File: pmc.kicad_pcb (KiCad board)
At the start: 6 copper layers, 52.1 x 93.3 mm, 167 parts, among them M1 TPS61040, M2 LM46001, M3 STM32F405RG, M4 REF3033, M5 TPS73633, M6 SN65HVD256, M7 UCC27211A, M8 UCC27211A, M9 UCC27211A, P1 FAN, P10 F1, P11 F2, P12 A1, P13 A2, P14 BOOT, P15 F1, P16 F2, P17 A1, P18 A2, P19 CONN4, P2 NTC, P20 CONN4, P21 CONN4, P22 CONN4, P23 CONN4, P3 HALL, P4 SPI, P5 PPM, P6 ANALOG, P7 CAN, P8 SWD, P9 USART, Q1 IRLML6401, Q2 IPT007N06N, Q3 IPT007N06N, Q4 IPT007N06N, Q5 IPT007N06N, Q6 IPT007N06N, Q7 IPT007N06N, U1 AD8539, U2 AD8539, U3 AD8417, U4 AD8417

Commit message: New mosfet driver and current sensing amp.
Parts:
- M7, M8, M9: value UCC27211A -> UCC27201A
- R47, R48: value 0.0003 1% -> 0.0005 1%
- U3, U4: value AD8417 -> AD8418
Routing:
- net GND: track 444.6 -> 445.9 mm, vias 228 -> 229
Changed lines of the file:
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@@
     (links 448)
     (no_connects 7)
-    (area 59.49 61.435 123.42 160.7915)
+    (area 60.249999 67.234999 112.470001 160.730001)
     (thickness 2)
     (drawings 109)
-    (tracks 2088)
+    (tracks 2091)
     (zones 0)
     (modules 167)
@@
   (title_block
     (title "Phobia Motor Controller")
-    (date 2019-04-27)
+    (date 2019-06-02)
     (rev 4c)
     (company "Roman Belov")
@@
   )
   (setup
-    (last_trace_width 0.508)
+    (last_trace_width 0.254)
     (user_trace_width 0.381)
     (user_trace_width 0.508)
@@
       (effects (font (size 0.635 0.635) (thickness 0.127)))
     )
-    (fp_text value UCC27211A (at 0 3.048 270) (layer F.SilkS) hide
+    (fp_text value UCC27201A (at 0 3.048 270) (layer F.SilkS) hide
       (effects (font (size 0.635 0.635) (thickness 0.127)))
     )
@@
       (effects (font (size 0.635 0.635) (thickness 0.127)))
     )
-    (fp_text value UCC27211A (at 0 3.048 270) (layer F.SilkS) hide
+    (fp_text value UCC27201A (at 0 3.048 270) (layer F.SilkS) hide
       (effects (font (size 0.635 0.635) (thickness 0.127)))
     )
@@
       (effects (font (size 0.635 0.635) (thickness 0.127)))
     )
-    (fp_text value UCC27211A (at -3.175 -5.08 270) (layer F.SilkS)
+    (fp_text value UCC27201A (at -3.175 -5.08 270) (layer F.SilkS)
       (effects (font (size 0.635 0.635) (thickness 0.127)))
     )
@@
       (effects (font (size 0.635 0.635) (thickness 0.127)))
     )
-    (fp_text value AD8417 (at 3.81 0 180) (layer F.SilkS)
+    (fp_text value AD8418 (at 3.81 0 180) (layer F.SilkS)
       (effects (font (size 0.635 0.635) (thickness 0.127)))
     )
@@
       (effects (font (size 0.635 0.635) (thickness 0.127)))
     )
-    (fp_text value AD8417 (at 3.81 0 180) (layer F.SilkS)
+    (fp_text value AD8418 (at 3.81 0 180) (layer F.SilkS)
       (effects (font (size 0.635 0.635) (thickness 0.127)))
     )
@@
       (effects (font (size 0.635 0.635) (thickness 0.127)))
     )
-    (fp_text value "0.0003 1%" (at 0.635 0.254 360) (layer F.SilkS)
+    (fp_text value "0.0005 1%" (at 0.635 0.254 360) (layer F.SilkS)
       (effects (font (size 0.635 0.635) (thickness 0.127)))
     )
@@
       (effects (font (size 0.635 0.635) (thickness 0.127)))
     )
-    (fp_text value "0.0003 1%" (at 0.635 0.254 360) (layer F.SilkS)
+    (fp_text value "0.0005 1%" (at 0.635 0.254 360) (layer F.SilkS)
       (effects (font (size 0.635 0.635) (thickness 0.127)))
     )
@@
   (segment (start 104.775 139.3825) (end 102.997 139.3825) (width 0.254) (layer F.Cu) (net 47))
   (segment (start 102.997 139.3825) (end 102.87 139.5095) (width 0.254) (layer F.Cu) (net 47))
+  (segment (start 69.723 135.255) (end 69.723 136.398) (width 0.254) (layer F.Cu) (net 49))
+  (segment (start 69.723 136.398) (end 69.85 136.525) (width 0.254) (layer F.Cu) (net 49))
+  (via (at 69.85 136.525) (size 0.300001) (drill 0.3) (layers F.Cu B.Cu) (net 49))
   (segment (start 74.4855 108.712) (end 76.0095 108.712) (width 0.381) (layer B.Cu) (net 49))
   (segment (start 76.0095 105.8545) (end 76.0095 108.712) (width 0.381) (layer B.Cu) (net 49))

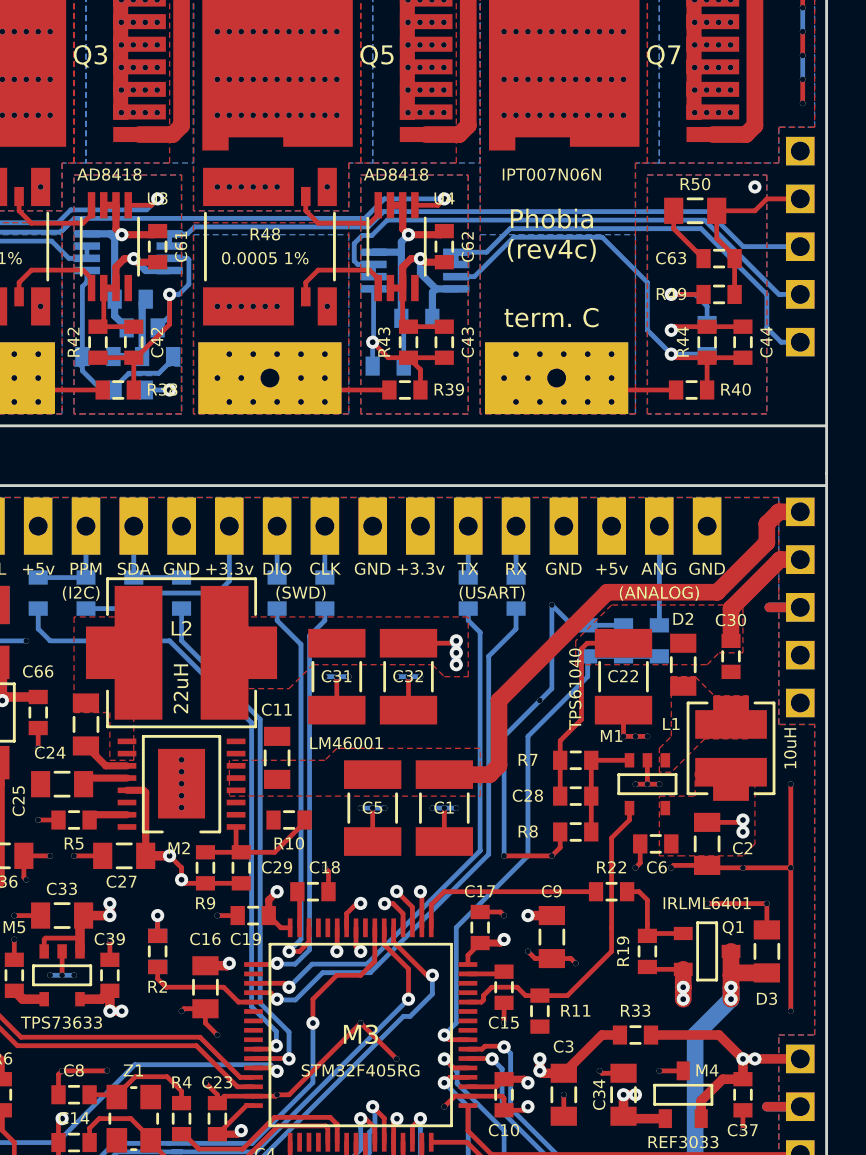
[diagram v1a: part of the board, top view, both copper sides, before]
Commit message: Two analog channels.
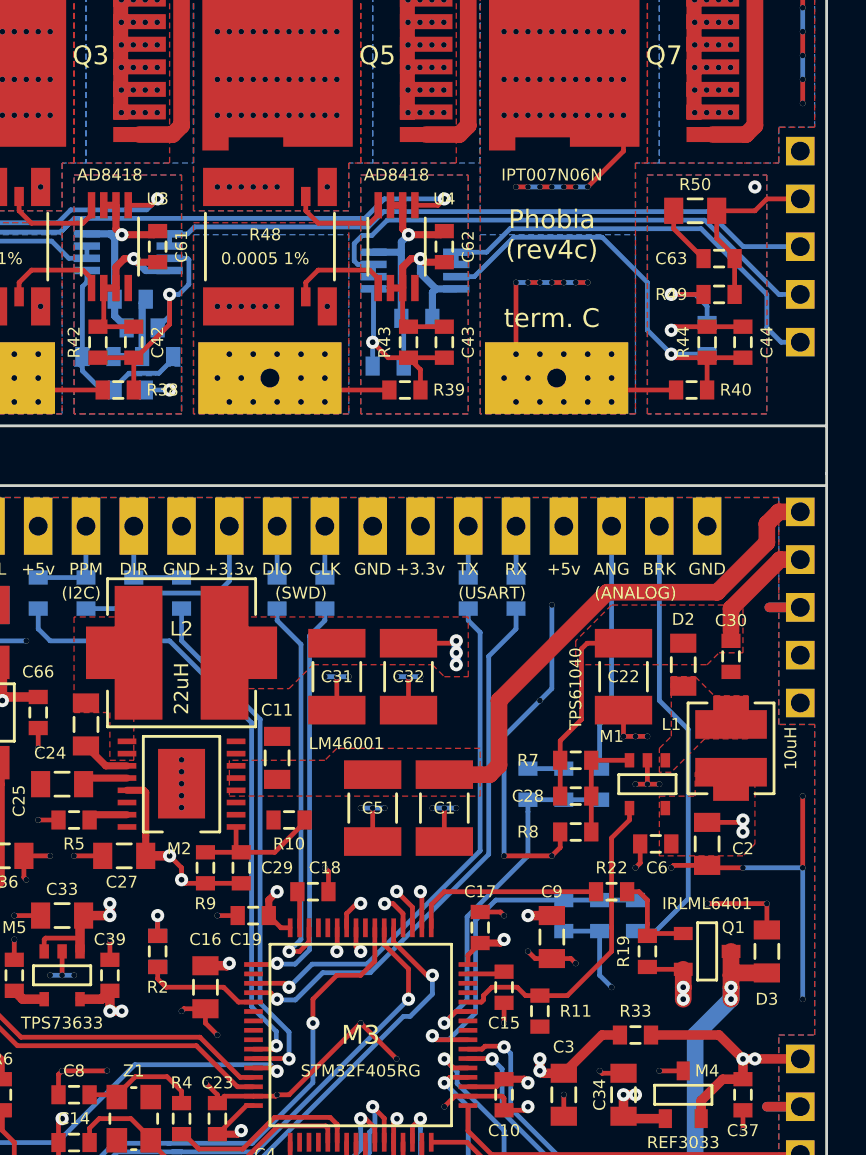
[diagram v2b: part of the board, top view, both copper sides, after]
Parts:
- added C67: 10nF 25v, foot:SM-0603, B.Cu at (98.4, 138.4)
- added R53: 10K 1%, foot:SM-0603, B.Cu at (100.3, 138.4)
- added R54: 10K 1%, foot:SM-0603, B.Cu at (102.2, 138.4)
- P6: footprint foot:PLS-3 -> foot:PLS-4
- P9: footprint foot:PLS-4 -> foot:PLS-3
- moved C40 8.25 mm to (96.5, 131.4)
- moved R34 8.25 mm to (98.4, 131.4)
- moved R36 8.25 mm to (100.3, 131.4)
- moved P6 1.27 mm to (102.2, 117.7)
- moved P9 1.27 mm to (93.3, 117.7)
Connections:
- C40 pad 2: ADC_IN14 -> ADC_IN9
- M3 pad 27: Net-(M3-Pad27) -> ADC_IN9
- P6 pad 3: GND -> Net-(P6-Pad3)
- R34 pad 2: ADC_IN14 -> ADC_IN9
- R36 pad 1: ADC_IN14 -> ADC_IN9
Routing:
- net Net-(P6-Pad3): track 0.00 -> 24.0 mm
- net TERMINAL_C: track 50.0 -> 69.3 mm, vias 58 -> 72
- net ADC_IN9: track 0.00 -> 19.2 mm, vias 0 -> 1
- net ADC_IN14: track 28.6 -> 18.8 mm
- net Net-(P6-Pad2): track 5.27 -> 13.2 mm
- net GND: track 445.9 -> 448.1 mm, vias 229 -> 230
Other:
- board text added: "BRK"
- board text added: "DIR"
- board text removed: "SDA"

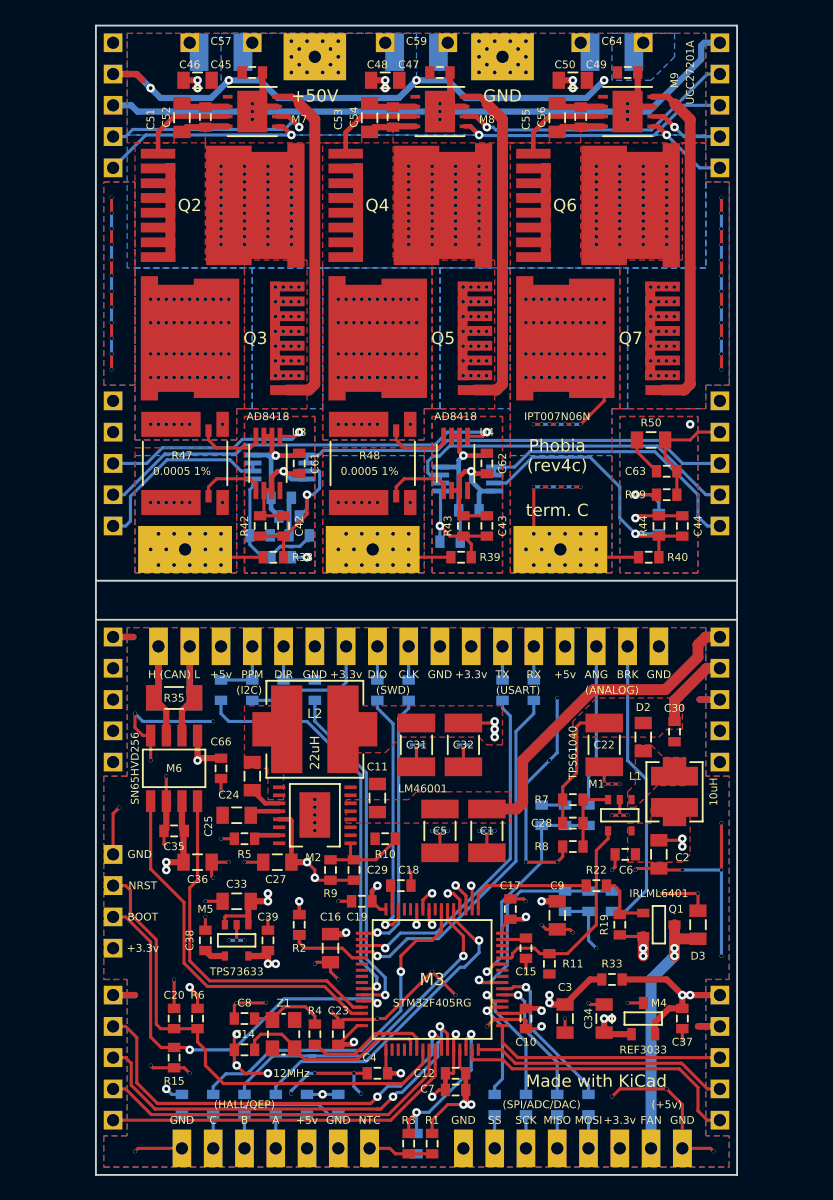
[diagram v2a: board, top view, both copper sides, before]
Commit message: Added mounting holes.
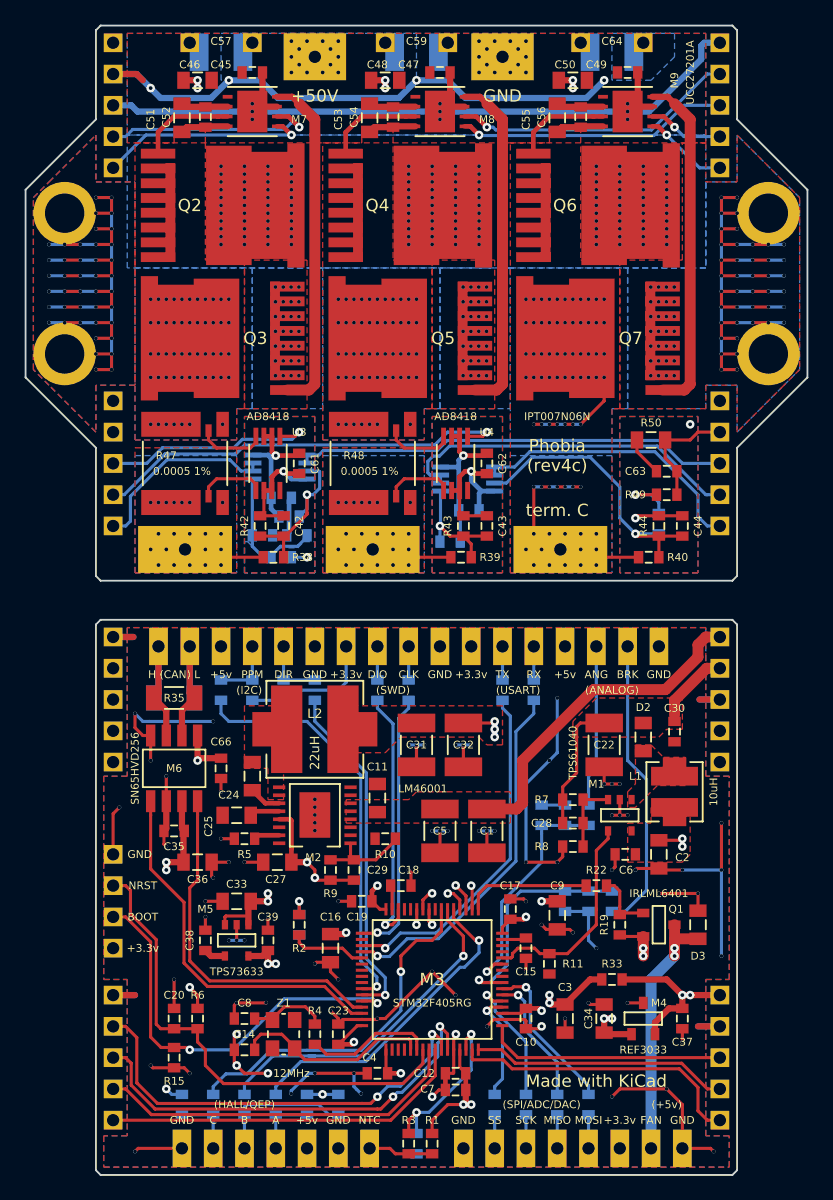
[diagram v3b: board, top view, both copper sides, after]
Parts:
- added PLS-1: VAL**, foot:PLS-1, F.Cu at (57.8, 94.0)
- added PLS-1: VAL**, foot:PLS-1, F.Cu at (114.9, 94.0)
- added PLS-1: VAL**, foot:PLS-1, F.Cu at (57.8, 82.5)
- added PLS-1: VAL**, foot:PLS-1, F.Cu at (114.9, 82.5)
- moved C41 0.19 mm to (73.9, 108.7)
- moved R41 0.19 mm to (76.6, 108.7)
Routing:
- net GND: track 448.1 -> 530.9 mm, vias 230 -> 290
- net +36V: track 188.9 -> 241.6 mm
- added copper zone on In6.Cu, net +3.3VREF
- added copper zone on In6.Cu, net +36V
- added copper zone on In6.Cu, net +5V
- added copper zone on In5.Cu, net GND
- added copper zone on In6.Cu, net GND
- added copper zone on In6.Cu, net Net-(C51-Pad1)
- added copper zone on In6.Cu, net Net-(C53-Pad1)
- added copper zone on In6.Cu, net TERMINAL_A
- added copper zone on In6.Cu, net TERMINAL_B
- added copper zone on In6.Cu, net TERMINAL_C
- removed copper zone on In4.Cu, net +3.3VREF
- removed copper zone on In4.Cu, net GND
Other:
- board size 52.1 x 93.3 mm -> 63.5 x 93.3 mm
- copper layers 6 -> 8

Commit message: Added heatsink drawing, CC attribution.
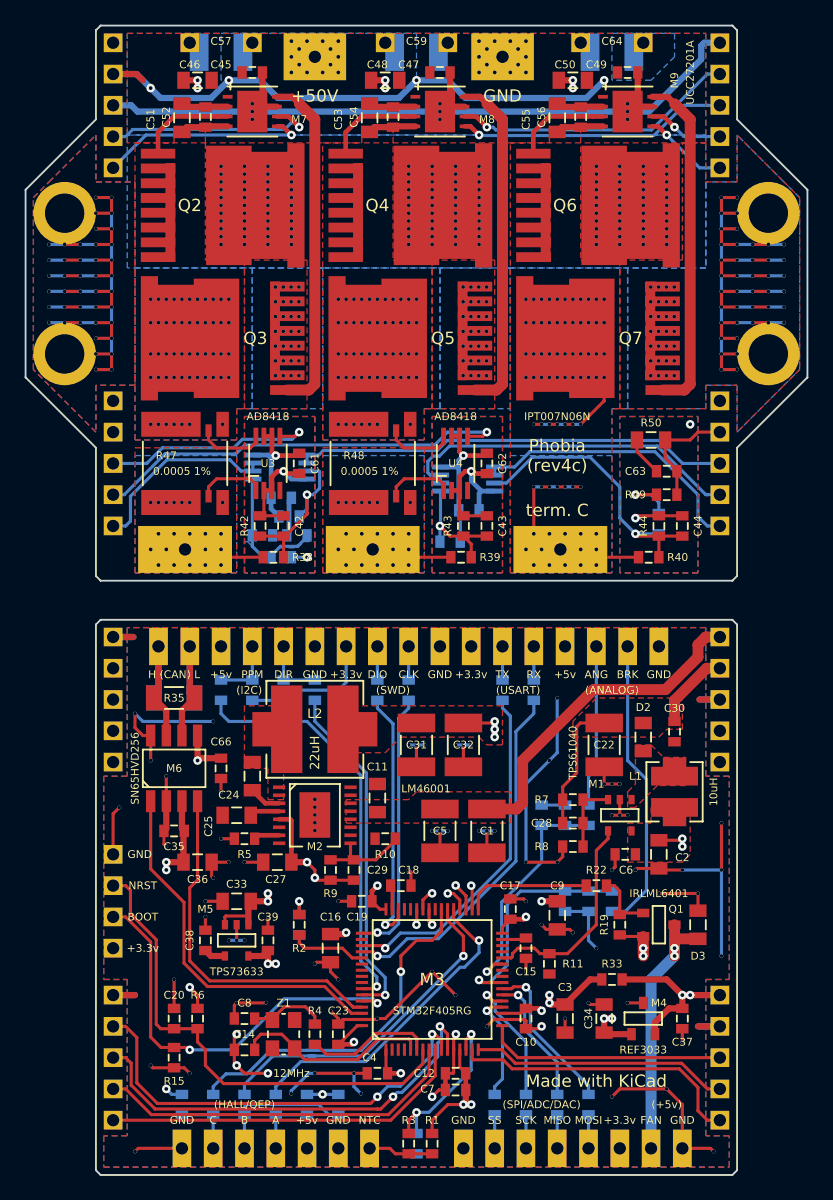
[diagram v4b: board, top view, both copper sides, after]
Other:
- board text added: "(CC-BY-SA)"
